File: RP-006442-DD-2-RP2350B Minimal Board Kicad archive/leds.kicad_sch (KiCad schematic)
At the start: 60 parts, among them U10 74HC595, U11 74HC595, U13 74HC595

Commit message: PNG and LCSC numbers
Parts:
- C43, C44, C48: LCSC (none) -> C1525
- R27, R28, R29, R30, R31, R32, R33, R34, R35, R36, R37, R38, R39, R40, R41, R42, R47, R48, R49, R50, R51, R52, R53, R54: LCSC (none) -> C25117
- U10, U11, U13: LCSC (none) -> C5947

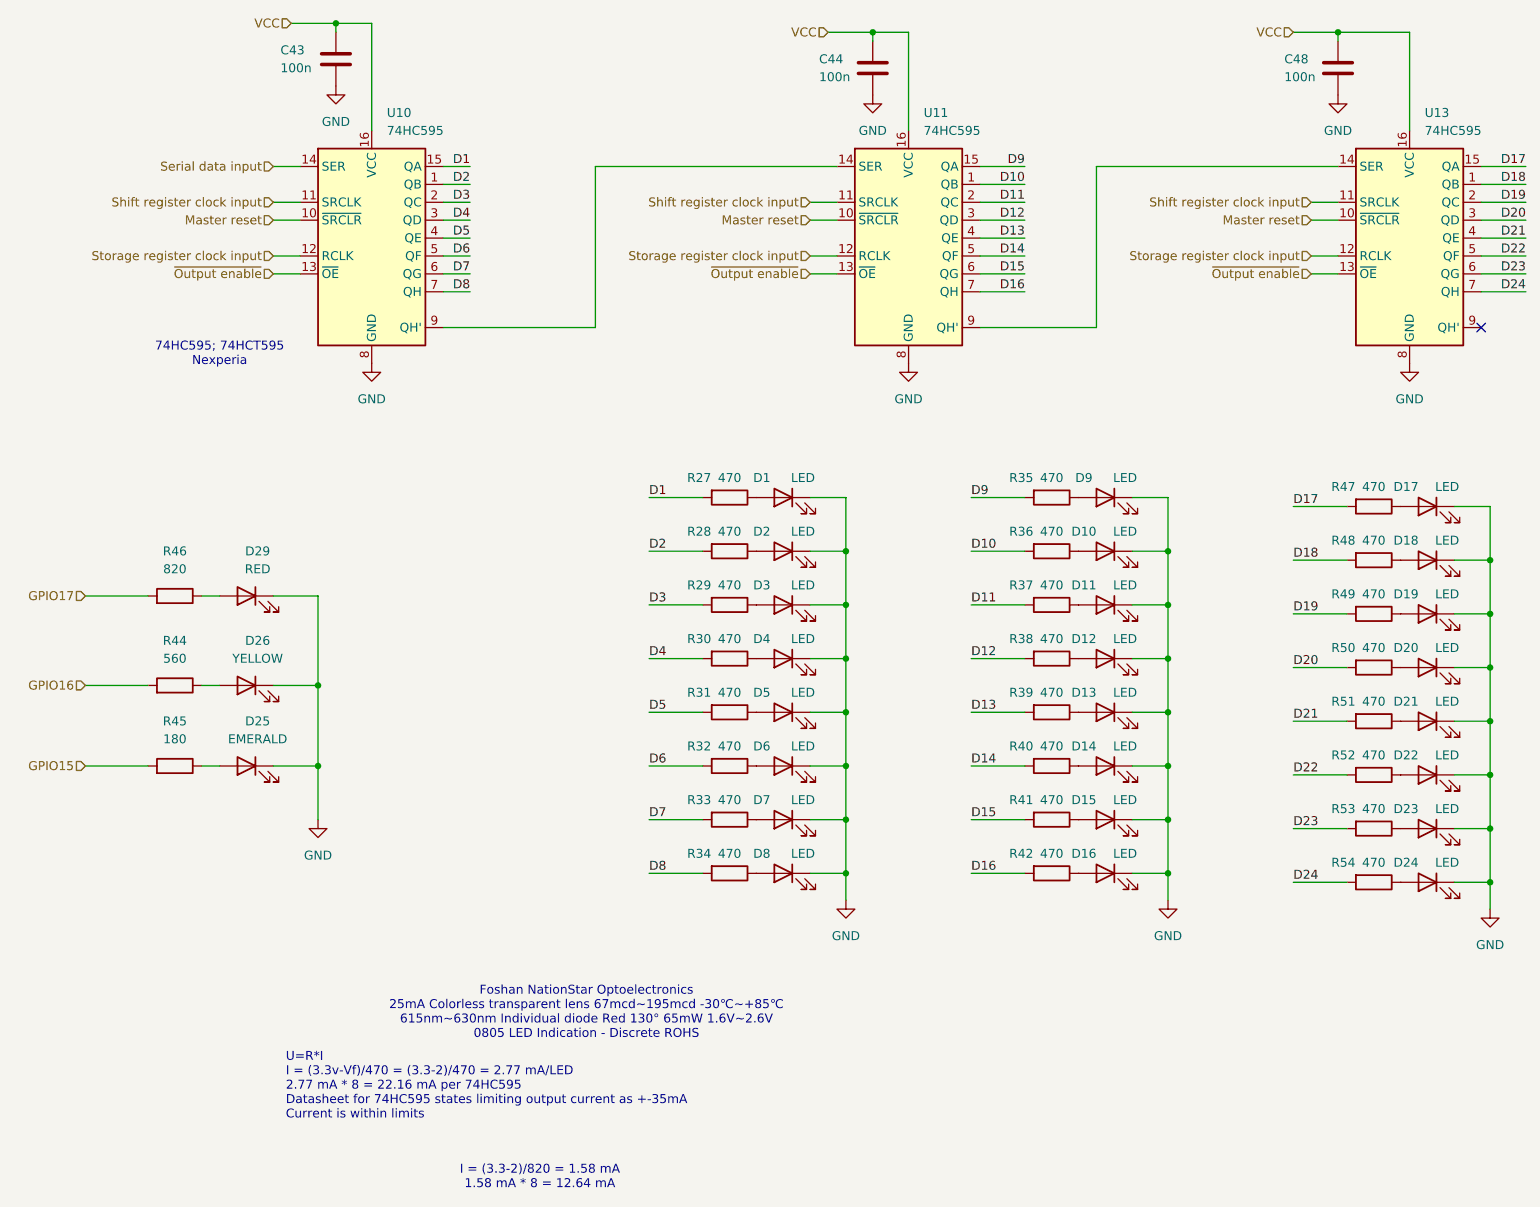
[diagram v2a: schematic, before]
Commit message: Added LCSC numbers to parts
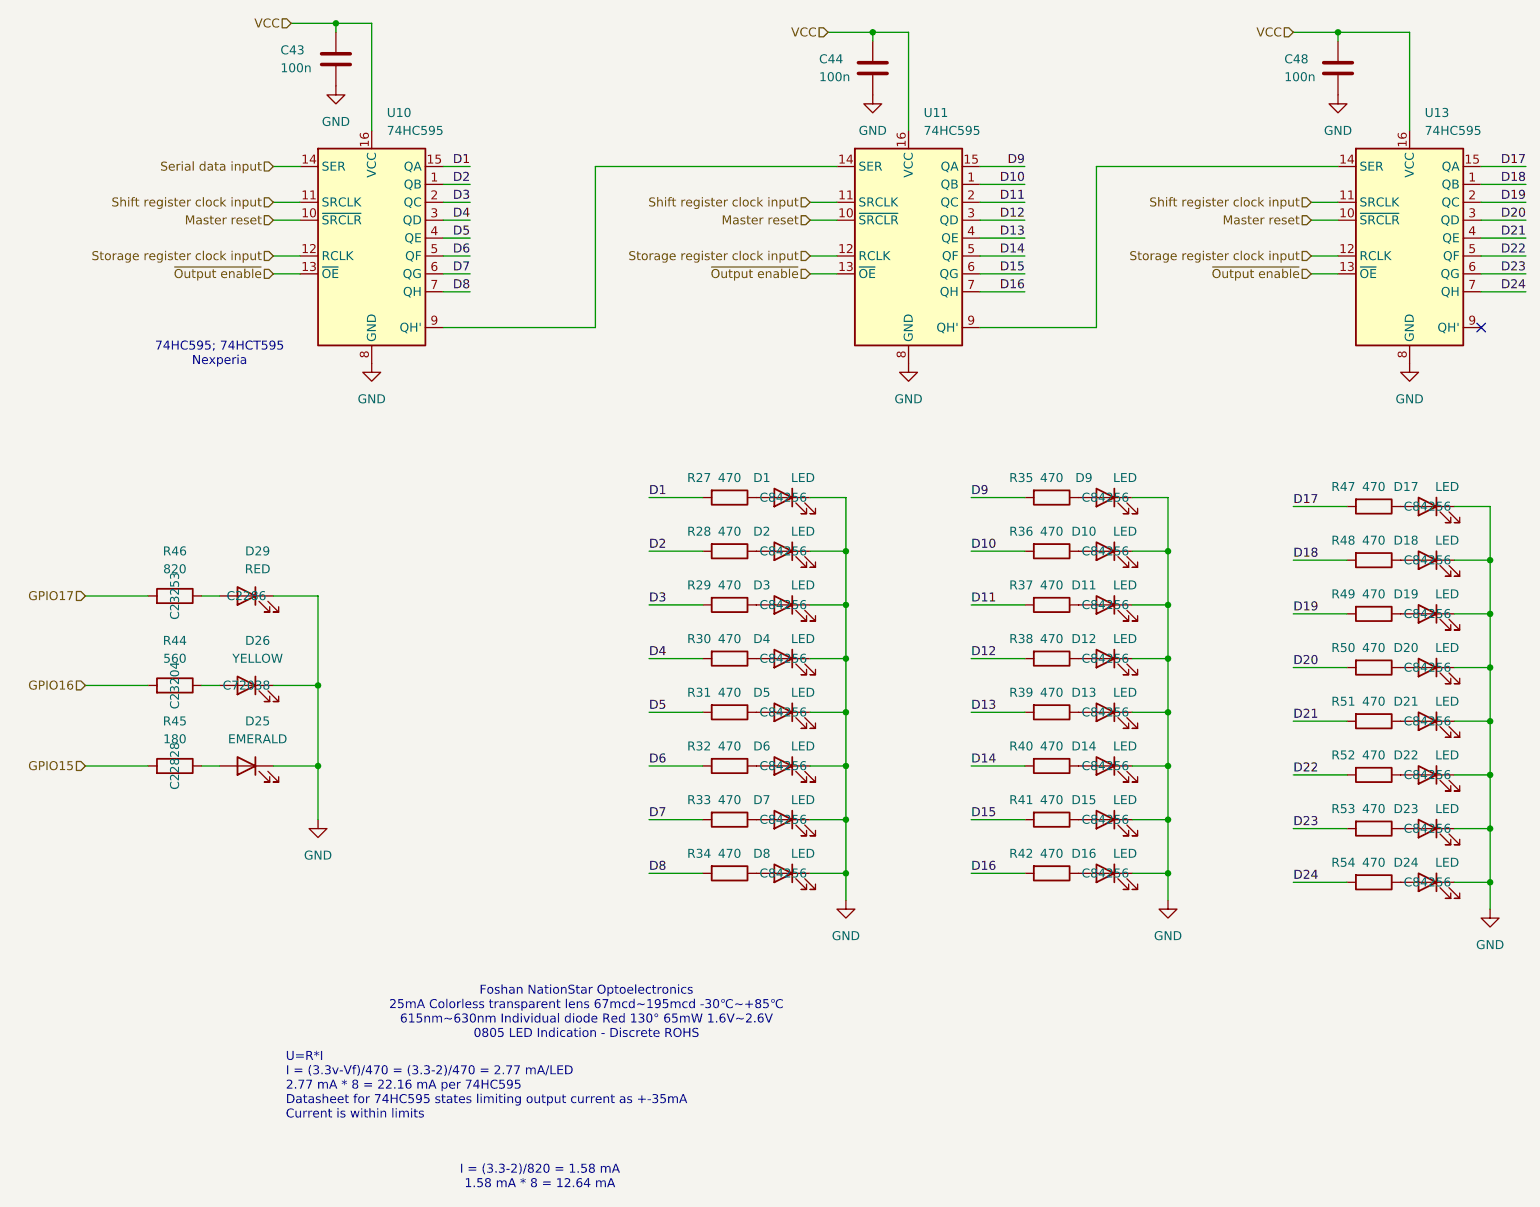
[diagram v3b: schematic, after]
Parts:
- D1, D10, D11, D12, D13, D14, D15, D16, D17, D18, D19, D2, D20, D21, D22, D23, D24, D3, D4, D5, D6, D7, D8, D9: LCSC (none) -> C84256
- D26: LCSC (none) -> C72038
- D29: LCSC (none) -> C2286
- R44: LCSC (none) -> C23204
- R45: LCSC (none) -> C22828
- R46: LCSC (none) -> C23253
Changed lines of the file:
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@@
 			)
 		)
+		(property "LCSC" "C84256"
+			(at 236.22 125.73 0)
+			(effects
+				(font
+					(size 1.27 1.27)
+				)
+			)
+		)
 		(pin "1"
 		)
@@
 			)
 		)
+		(property "LCSC" "C84256"
+			(at 144.78 93.98 0)
+			(effects
+				(font
+					(size 1.27 1.27)
+				)
+			)
+		)
 		(pin "1"
 		)
@@
 			)
 		)
+		(property "LCSC" "C84256"
+			(at 144.78 86.36 0)
+			(effects
+				(font
+					(size 1.27 1.27)
+				)
+			)
+		)
 		(pin "1"
 		)
@@
 			)
 		)
+		(property "LCSC" "C84256"
+			(at 190.5 109.22 0)
+			(effects
+				(font
+					(size 1.27 1.27)
+				)
+			)
+		)
 		(pin "1"
 		)
@@
 			)
 		)
+		(property "LCSC" "C84256"
+			(at 144.78 132.08 0)
+			(effects
+				(font
+					(size 1.27 1.27)
+				)
+			)
+		)
 		(pin "1"
 		)
@@
 			)
 		)
+		(property "LCSC" "C84256"
+			(at 190.5 124.46 0)
+			(effects
+				(font
+					(size 1.27 1.27)
+				)
+			)
+		)
 		(pin "1"
 		)
@@
 			)
 		)
+		(property "LCSC" "C72038"
+			(at 68.58 113.03 0)
+			(effects
+				(font
+					(size 1.27 1.27)
+				)
+			)
+		)
 		(pin "1"
 		)
@@
 			)
 		)
+		(property "LCSC" "C84256"
+			(at 144.78 101.6 0)
+			(effects
+				(font
+					(size 1.27 1.27)
+				)
+			)
+		)
 		(pin "1"
 		)
@@
 			)
 		)
+		(property "LCSC" "C84256"
+			(at 236.22 133.35 0)
+			(effects
+				(font
+					(size 1.27 1.27)
+				)
+			)
+		)
 		(pin "1"
 		)
@@
 			)
 		)
+		(property "LCSC" "C84256"
+			(at 190.5 116.84 0)
+			(effects
+				(font
+					(size 1.27 1.27)
+				)
+			)
+		)
 		(pin "1"
 		)
@@
 			)
 		)
+		(property "LCSC" "C84256"
+			(at 144.78 116.84 0)
+			(effects
+				(font
+					(size 1.27 1.27)
+				)
+			)
+		)
 		(pin "1"
 		)
@@
 			)
 		)
+		(property "LCSC" "C84256"
+			(at 144.78 139.7 0)
+			(effects
+				(font
+					(size 1.27 1.27)
+				)
+			)
+		)
 		(pin "1"
 		)
@@
 			)
 		)
+		(property "LCSC" "C84256"
+			(at 236.22 118.11 0)
+			(effects
+				(font
+					(size 1.27 1.27)
+				)
+			)
+		)
 		(pin "1"
 		)
@@
 			)
 		)
+		(property "LCSC" "C84256"
+			(at 190.5 132.08 0)
+			(effects
+				(font
+					(size 1.27 1.27)
+				)
+			)
+		)
 		(pin "1"
 		)
@@
 			)
 		)
+		(property "LCSC" "C84256"
+			(at 190.5 101.6 0)
+			(effects
+				(font
+					(size 1.27 1.27)
+				)
+			)
+		)
 		(pin "1"
 		)
@@
 			)
 		)
+		(property "LCSC" "C84256"
+			(at 236.22 110.49 0)
+			(effects
+				(font
+					(size 1.27 1.27)
+				)
+			)
+		)
 		(pin "1"
 		)
@@
 			)
 		)
+		(property "LCSC" "C84256"
+			(at 236.22 102.87 0)
+			(effects
+				(font
+					(size 1.27 1.27)
+				)
+			)
+		)
 		(pin "1"
 		)
@@
 			)
 		)
+		(property "LCSC" "C84256"
+			(at 144.78 124.46 0)
+			(effects
+				(font
+					(size 1.27 1.27)
+				)
+			)
+		)
 		(pin "1"
 		)
@@
 			)
 		)
+		(property "LCSC" "C84256"
+			(at 190.5 93.98 0)
+			(effects
+				(font
+					(size 1.27 1.27)
+				)
+			)
+		)
 		(pin "1"
 		)
@@
 			)
 		)
+		(property "LCSC" "C84256"
+			(at 236.22 87.63 0)
+			(effects
+				(font
+					(size 1.27 1.27)
+				)
+			)
+		)
 		(pin "1"
 		)
@@
 			)
 		)
+		(property "LCSC" "C22828"
+			(at 58.42 124.46 0)
+			(effects
+				(font
+					(size 1.27 1.27)
+				)
+			)
+		)
 		(pin "1"
 		)
@@
 			)
 		)
+		(property "LCSC" "C23204"
+			(at 58.42 113.03 0)
+			(effects
+				(font
+					(size 1.27 1.27)
+				)
+			)
+		)
 		(pin "2"
 		)
@@
 			)
 		)
+		(property "LCSC" "C84256"
+			(at 144.78 109.22 0)
+			(effects
+				(font
+					(size 1.27 1.27)
+				)
+			)
+		)
 		(pin "1"
 		)
@@
 			)
 		)
+		(property "LCSC" "C84256"
+			(at 236.22 95.25 0)
+			(effects
+				(font
+					(size 1.27 1.27)
+				)
+			)
+		)
 		(pin "1"
 		)
@@
 			)
 		)
+		(property "LCSC" "C2286"
+			(at 68.58 100.33 0)
+			(effects
+				(font
+					(size 1.27 1.27)
+				)
+			)
+		)
 		(pin "1"
 		)
@@
 			)
 		)
+		(property "LCSC" "C84256"
+			(at 190.5 139.7 0)
+			(effects
+				(font
+					(size 1.27 1.27)
+				)
+			)
+		)
 		(pin "1"
 		)
@@
 			)
 		)
+		(property "LCSC" "C84256"
+			(at 190.5 86.36 0)
+			(effects
+				(font
+					(size 1.27 1.27)
+				)
+			)
+		)
 		(pin "1"
 		)
@@
 			)
 		)
+		(property "LCSC" "C23253"
+			(at 58.42 100.33 0)
+			(effects
+				(font
+					(size 1.27 1.27)
+				)
+			)
+		)
 		(pin "2"
 		)
@@
 			)
 		)
+		(property "LCSC" "C84256"
+			(at 236.22 140.97 0)
+			(effects
+				(font
+					(size 1.27 1.27)
+				)
+			)
+		)

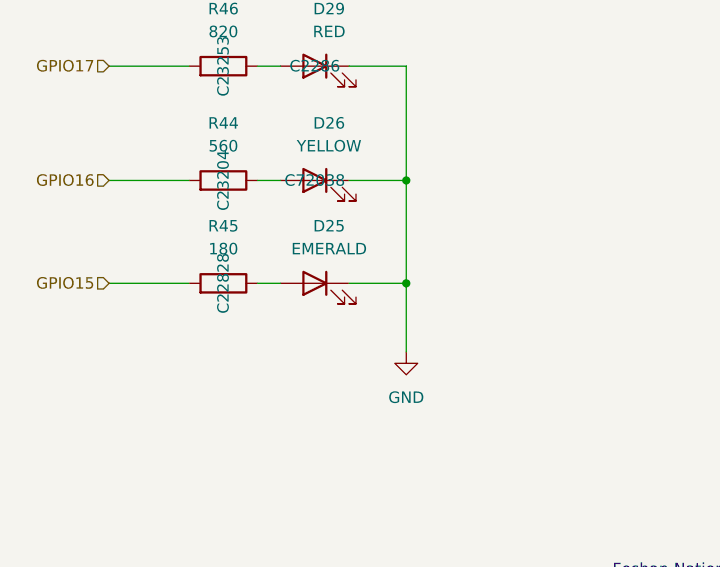
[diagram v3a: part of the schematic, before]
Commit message: Added Emerald LED LCSC number
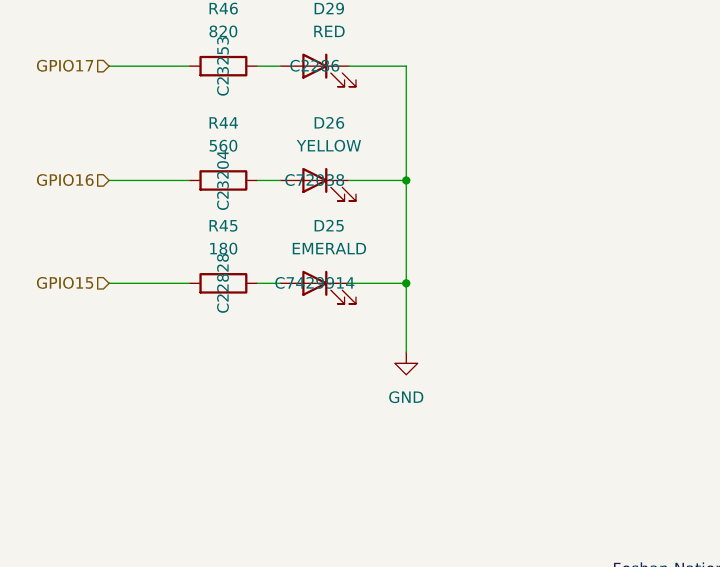
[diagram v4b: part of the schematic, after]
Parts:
- D25: LCSC (none) -> C7429914
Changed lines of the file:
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@@
+			)
+		)
+		(property "LCSC" "C7429914"
+			(at 68.58 124.46 0)
+			(effects
+				(font
+					(size 1.27 1.27)
+				)
 			)
 		)
